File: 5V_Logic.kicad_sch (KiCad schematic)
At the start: 13 parts

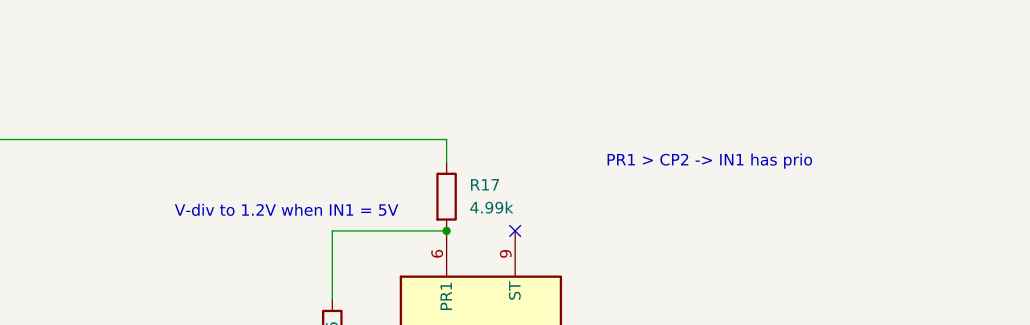
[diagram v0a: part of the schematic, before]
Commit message: tried to find some placements for power routing
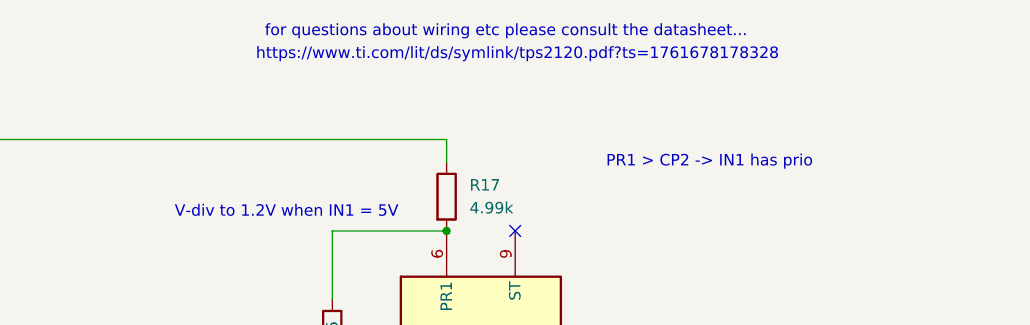
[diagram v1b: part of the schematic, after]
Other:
- note added: "for questions about wiring etc please consult the datasheet..."
- note added: "https://www.ti.com/lit/ds/symlink/tps2120.pdf?ts=1761678178328"
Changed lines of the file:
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@@
 	(generator_version "9.0")
 	(paper "A4")
+	(text "for questions about wiring etc please consult the datasheet..."
+		(exclude_from_sim no)
+		(at 148.844 49.022 0)
+		(effects
+			(font
+				(size 1.27 1.27)
+			)
+		)
+	)
 	(text "V-div to 1.2V when IN1 = 5V"
 		(exclude_from_sim no)
@@
 		(effects
 			(font
+				(size 1.27 1.27)
+			)
+		)
+	)
+	(text "https://www.ti.com/lit/ds/symlink/tps2120.pdf?ts=1761678178328"
+		(exclude_from_sim no)
+		(at 150.114 51.562 0)
+		(effects
+			(font

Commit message: added Gyroscope and Accelerometer part (4x) over IIC
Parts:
- IC3: value ~ -> TPS2121RUXT
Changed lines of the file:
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@@
 			)
 		)
-		(property "Value" "~"
+		(property "Value" "TPS2121RUXT"
 			(at 146.05 119.38 0)
 			(effects

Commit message: multiple chainges on PCB
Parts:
- IC3: Order (none) -> Ordered=True
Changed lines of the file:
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@@
+			)
+		)
+		(property "Order" "Ordered=True"
+			(at 132.08 86.36 0)
+			(effects
+				(font
+					(size 1.27 1.27)
+				)
+				(hide yes)
 			)
 		)

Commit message: Power changes
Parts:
- renumbered C21 to C28, C22 to C29, C23 to C30, C24 to C31, C25 to C32, C26 to C33, C27 to C34, IC3 to IC4, R16 to R20, R17 to R21, R18 to R22, R19 to R23, R20 to R24
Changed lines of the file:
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@@
 		(dnp no)
 		(fields_autoplaced yes)
-		(property "Reference" "#PWR031"
+		(property "Reference" "#PWR017"
 			(at 168.91 127 0)
 			(effects
@@
 		)
 		(instances
-			(project ""
-				(path "/ce1819b2-f280-40ed-834f-6fe4d12f809d/c1998c4d-3f9a-4761-b447-a813532738a0/7fd5a03c-dea9-4dd3-96f2-bf31ea6dc8ac"
-					(reference "#PWR031")
+			(project "nautilus_mainboard"
+				(path "/ce1819b2-f280-40ed-834f-6fe4d12f809d/c1998c4d-3f9a-4761-b447-a813532738a0/3997d1c1-5566-40cd-ab06-9f3399d8a463"
+					(reference "#PWR017")
 					(unit 1)
 				)
@@
 		(on_board yes)
 		(dnp no)
-		(property "Reference" "C27"
+		(property "Reference" "C34"
 			(at 171.196 87.884 0)
 			(effects
@@
 		)
 		(instances
-			(project ""
-				(path "/ce1819b2-f280-40ed-834f-6fe4d12f809d/c1998c4d-3f9a-4761-b447-a813532738a0/7fd5a03c-dea9-4dd3-96f2-bf31ea6dc8ac"
-					(reference "C27")
+			(project "nautilus_mainboard"
+				(path "/ce1819b2-f280-40ed-834f-6fe4d12f809d/c1998c4d-3f9a-4761-b447-a813532738a0/3997d1c1-5566-40cd-ab06-9f3399d8a463"
+					(reference "C34")
 					(unit 1)
 				)
@@
 		(on_board yes)
 		(dnp no)
-		(property "Reference" "C24"
+		(property "Reference" "C31"
 			(at 123.698 103.378 0)
 			(effects
@@
 		(instances
 			(project "nautilus_mainboard"
-				(path "/ce1819b2-f280-40ed-834f-6fe4d12f809d/c1998c4d-3f9a-4761-b447-a813532738a0/7fd5a03c-dea9-4dd3-96f2-bf31ea6dc8ac"
-					(reference "C24")
+				(path "/ce1819b2-f280-40ed-834f-6fe4d12f809d/c1998c4d-3f9a-4761-b447-a813532738a0/3997d1c1-5566-40cd-ab06-9f3399d8a463"
+					(reference "C31")
 					(unit 1)
 				)
@@
 		(dnp no)
 		(fields_autoplaced yes)
-		(property "Reference" "R20"
+		(property "Reference" "R24"
 			(at 179.07 104.1399 0)
 			(effects
@@
 		)
 		(instances
-			(project ""
-				(path "/ce1819b2-f280-40ed-834f-6fe4d12f809d/c1998c4d-3f9a-4761-b447-a813532738a0/7fd5a03c-dea9-4dd3-96f2-bf31ea6dc8ac"
-					(reference "R20")
+			(project "nautilus_mainboard"
+				(path "/ce1819b2-f280-40ed-834f-6fe4d12f809d/c1998c4d-3f9a-4761-b447-a813532738a0/3997d1c1-5566-40cd-ab06-9f3399d8a463"
+					(reference "R24")
 					(unit 1)
 				)
@@
 		(on_board yes)
 		(dnp no)
-		(property "Reference" "R18"
+		(property "Reference" "R22"
 			(at 168.91 103.886 90)
 			(effects
@@
 		)
 		(instances
-			(project ""
-				(path "/ce1819b2-f280-40ed-834f-6fe4d12f809d/c1998c4d-3f9a-4761-b447-a813532738a0/7fd5a03c-dea9-4dd3-96f2-bf31ea6dc8ac"
-					(reference "R18")
+			(project "nautilus_mainboard"
+				(path "/ce1819b2-f280-40ed-834f-6fe4d12f809d/c1998c4d-3f9a-4761-b447-a813532738a0/3997d1c1-5566-40cd-ab06-9f3399d8a463"
+					(reference "R22")
 					(unit 1)
 				)
@@
 		(on_board yes)
 		(dnp no)
-		(property "Reference" "C26"
+		(property "Reference" "C33"
 			(at 163.068 88.392 0)
 			(effects
@@
 		(instances
 			(project "nautilus_mainboard"
-				(path "/ce1819b2-f280-40ed-834f-6fe4d12f809d/c1998c4d-3f9a-4761-b447-a813532738a0/7fd5a03c-dea9-4dd3-96f2-bf31ea6dc8ac"
-					(reference "C26")
+				(path "/ce1819b2-f280-40ed-834f-6fe4d12f809d/c1998c4d-3f9a-4761-b447-a813532738a0/3997d1c1-5566-40cd-ab06-9f3399d8a463"
+					(reference "C33")
 					(unit 1)
 				)
@@
 		(on_board yes)
 		(dnp no)
-		(property "Reference" "C23"
+		(property "Reference" "C30"
 			(at 123.952 88.392 0)
 			(effects
@@
 		)
 		(instances
-			(project ""
-				(path "/ce1819b2-f280-40ed-834f-6fe4d12f809d/c1998c4d-3f9a-4761-b447-a813532738a0/7fd5a03c-dea9-4dd3-96f2-bf31ea6dc8ac"
-					(reference "C23")
+			(project "nautilus_mainboard"
+				(path "/ce1819b2-f280-40ed-834f-6fe4d12f809d/c1998c4d-3f9a-4761-b447-a813532738a0/3997d1c1-5566-40cd-ab06-9f3399d8a463"
+					(reference "C30")
 					(unit 1)
 				)
@@
 		(dnp no)
 		(fields_autoplaced yes)
-		(property "Reference" "R17"
+		(property "Reference" "R21"
 			(at 144.78 66.0399 0)
 			(effects
@@
 		)
 		(instances
-			(project ""
-				(path "/ce1819b2-f280-40ed-834f-6fe4d12f809d/c1998c4d-3f9a-4761-b447-a813532738a0/7fd5a03c-dea9-4dd3-96f2-bf31ea6dc8ac"
-					(reference "R17")
+			(project "nautilus_mainboard"
+				(path "/ce1819b2-f280-40ed-834f-6fe4d12f809d/c1998c4d-3f9a-4761-b447-a813532738a0/3997d1c1-5566-40cd-ab06-9f3399d8a463"
+					(reference "R21")
 					(unit 1)
 				)
@@
 		(dnp no)
 		(fields_autoplaced yes)
-		(property "Reference" "R19"
+		(property "Reference" "R23"
 			(at 179.07 96.5199 0)
 			(effects
@@
 		(instances
 			(project "nautilus_mainboard"
-				(path "/ce1819b2-f280-40ed-834f-6fe4d12f809d/c1998c4d-3f9a-4761-b447-a813532738a0/7fd5a03c-dea9-4dd3-96f2-bf31ea6dc8ac"
-					(reference "R19")
+				(path "/ce1819b2-f280-40ed-834f-6fe4d12f809d/c1998c4d-3f9a-4761-b447-a813532738a0/3997d1c1-5566-40cd-ab06-9f3399d8a463"
+					(reference "R23")
 					(unit 1)
 				)
@@
 		(on_board yes)
 		(dnp no)
-		(property "Reference" "C25"
+		(property "Reference" "C32"
 			(at 163.83 106.68 90)
 			(effects
@@
 		)
 		(instances
-			(project ""
-				(path "/ce1819b2-f280-40ed-834f-6fe4d12f809d/c1998c4d-3f9a-4761-b447-a813532738a0/7fd5a03c-dea9-4dd3-96f2-bf31ea6dc8ac"
-					(reference "C25")
+			(project "nautilus_mainboard"
+				(path "/ce1819b2-f280-40ed-834f-6fe4d12f809d/c1998c4d-3f9a-4761-b447-a813532738a0/3997d1c1-5566-40cd-ab06-9f3399d8a463"
+					(reference "C32")
 					(unit 1)
 				)
@@
 		(dnp no)
 		(fields_autoplaced yes)
-		(property "Reference" "IC3"
+		(property "Reference" "IC4"
 			(at 146.05 116.84 0)
 			(effects
@@
 		)
 		(instances
-			(project ""
-				(path "/ce1819b2-f280-40ed-834f-6fe4d12f809d/c1998c4d-3f9a-4761-b447-a813532738a0/7fd5a03c-dea9-4dd3-96f2-bf31ea6dc8ac"
-					(reference "IC3")
+			(project "nautilus_mainboard"
+				(path "/ce1819b2-f280-40ed-834f-6fe4d12f809d/c1998c4d-3f9a-4761-b447-a813532738a0/3997d1c1-5566-40cd-ab06-9f3399d8a463"
+					(reference "IC4")
 					(unit 1)
 				)
@@
 		(on_board yes)
 		(dnp no)
-		(property "Reference" "C21"
+		(property "Reference" "C28"
 			(at 115.316 87.884 0)
 			(effects
@@
 		)
 		(instances
-			(project ""
-				(path "/ce1819b2-f280-40ed-834f-6fe4d12f809d/c1998c4d-3f9a-4761-b447-a813532738a0/7fd5a03c-dea9-4dd3-96f2-bf31ea6dc8ac"
-					(reference "C21")
+			(project "nautilus_mainboard"
+				(path "/ce1819b2-f280-40ed-834f-6fe4d12f809d/c1998c4d-3f9a-4761-b447-a813532738a0/3997d1c1-5566-40cd-ab06-9f3399d8a463"
+					(reference "C28")
 					(unit 1)
 				)
@@
 		(on_board yes)
 		(dnp no)
-		(property "Reference" "R16"
+		(property "Reference" "R20"
 			(at 129.54 84.582 90)
 			(effects
@@
 		)
 		(instances
-			(project ""
-				(path "/ce1819b2-f280-40ed-834f-6fe4d12f809d/c1998c4d-3f9a-4761-b447-a813532738a0/7fd5a03c-dea9-4dd3-96f2-bf31ea6dc8ac"
-					(reference "R16")
+			(project "nautilus_mainboard"
+				(path "/ce1819b2-f280-40ed-834f-6fe4d12f809d/c1998c4d-3f9a-4761-b447-a813532738a0/3997d1c1-5566-40cd-ab06-9f3399d8a463"
+					(reference "R20")
 					(unit 1)
 				)
@@
 		(on_board yes)
 		(dnp no)
-		(property "Reference" "C22"
+		(property "Reference" "C29"
 			(at 115.316 103.124 0)
 			(effects
@@
 		(instances
 			(project "nautilus_mainboard"
-				(path "/ce1819b2-f280-40ed-834f-6fe4d12f809d/c1998c4d-3f9a-4761-b447-a813532738a0/7fd5a03c-dea9-4dd3-96f2-bf31ea6dc8ac"
-					(reference "C22")
+				(path "/ce1819b2-f280-40ed-834f-6fe4d12f809d/c1998c4d-3f9a-4761-b447-a813532738a0/3997d1c1-5566-40cd-ab06-9f3399d8a463"
+					(reference "C29")
 					(unit 1)
 				)

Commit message: chore: more cleanup
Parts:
- removed C28, C29: 10uF, Capacitor_SMD:C_1210_3225Metric, symbol #dzdb:s_cap/C-MUR-GRM32EC72A106KE05
- removed C30, C31, C33: 100nF, Capacitor_SMD:C_0603_1608Metric, symbol #dzdb:g_cap/C-100n-0603
- removed C32: 330nF, Capacitor_SMD:C_0603_1608Metric, symbol #dzdb:g_cap/C-330n-0603
- removed C34: 47uF, Capacitor_SMD:C_0805_2012Metric, symbol #dzdb:s_cap/C-MUR-GRM21BR61A476ME15
- removed IC4: TPS2121RUXT, dz_dio:TI_Switchover_TPS2121RUXT, symbol #dzdb:s_misc/TEXA-595-TPS2121RUXT
- removed R20: 15.4k, Resistor_SMD:R_0603_1608Metric, symbol #dzdb:g_res/R-15.4k-0603
- removed R21, R23: 4.99k, Resistor_SMD:R_0603_1608Metric, symbol #dzdb:g_res/R-4.99k-0603
- removed R24: 20k, Resistor_SMD:R_0603_1608Metric, symbol #dzdb:g_res/R-20k-0603
- added C35, C36: 10uF, Capacitor_SMD:C_1210_3225Metric, symbol #dzdb:s_cap/C-MUR-GRM32EC72A106KE05
- added C37, C38, C40: 100nF, Capacitor_SMD:C_0603_1608Metric, symbol #dzdb:g_cap/C-100n-0603
- added C41: 330nF, Capacitor_SMD:C_0603_1608Metric, symbol #dzdb:g_cap/C-330n-0603
- added C53: 47uF, Capacitor_SMD:C_0805_2012Metric, symbol #dzdb:s_cap/C-MUR-GRM21BR61A476ME15
- added IC5: TPS2121RUXT, dz_dio:TI_Switchover_TPS2121RUXT, symbol #dzdb:s_misc/TEXA-595-TPS2121RUXT
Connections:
- net Battery_Out_5V: now also C35.1, C37.1, IC5.6 (PR1), IC5.7 (IN1)
- net CM4_In_5V: now also C40.1, C53.1, IC5.1 (OUT_1), IC5.8 (OUT_2)
- net GND: now also R22.1, C35.2, C36.2, C37.2, C38.2, C40.2, C41.1, C53.2, IC5.12 (GND), IC5.3 (CP2), IC5.4 (OV2), IC5.5 (OV1); no longer R22.2
- net USB_Out_5V: now also C36.1, C38.1, IC5.2 (IN2)
- new net: C41.2, IC5.11 (SS)
- new net: IC5.10 (ILIM), R22.2
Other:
- note removed: "V-div to 1.2V when IN1 = 5V"
- note removed: "V-div to 1V when IN2=5V"
- note removed: "wrong caps. 100nf + 10myF"
- company: (none) -> Davide
- moved on the sheet: R22

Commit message: chore: Loads of redoing stuff. Added a Changelog
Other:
- title: (none) -> Nautilus_Mainboard
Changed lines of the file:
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@@
 	(paper "A4")
 	(title_block
+		(title "Nautilus_Mainboard")
 		(date "2025-11-19")
 		(rev "0")
